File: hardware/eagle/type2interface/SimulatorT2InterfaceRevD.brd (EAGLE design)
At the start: 80 x 80 mm, 25 parts, among them IC1 7805T, IC2 MAX233, IC3 ATMEGA328P_PDIP

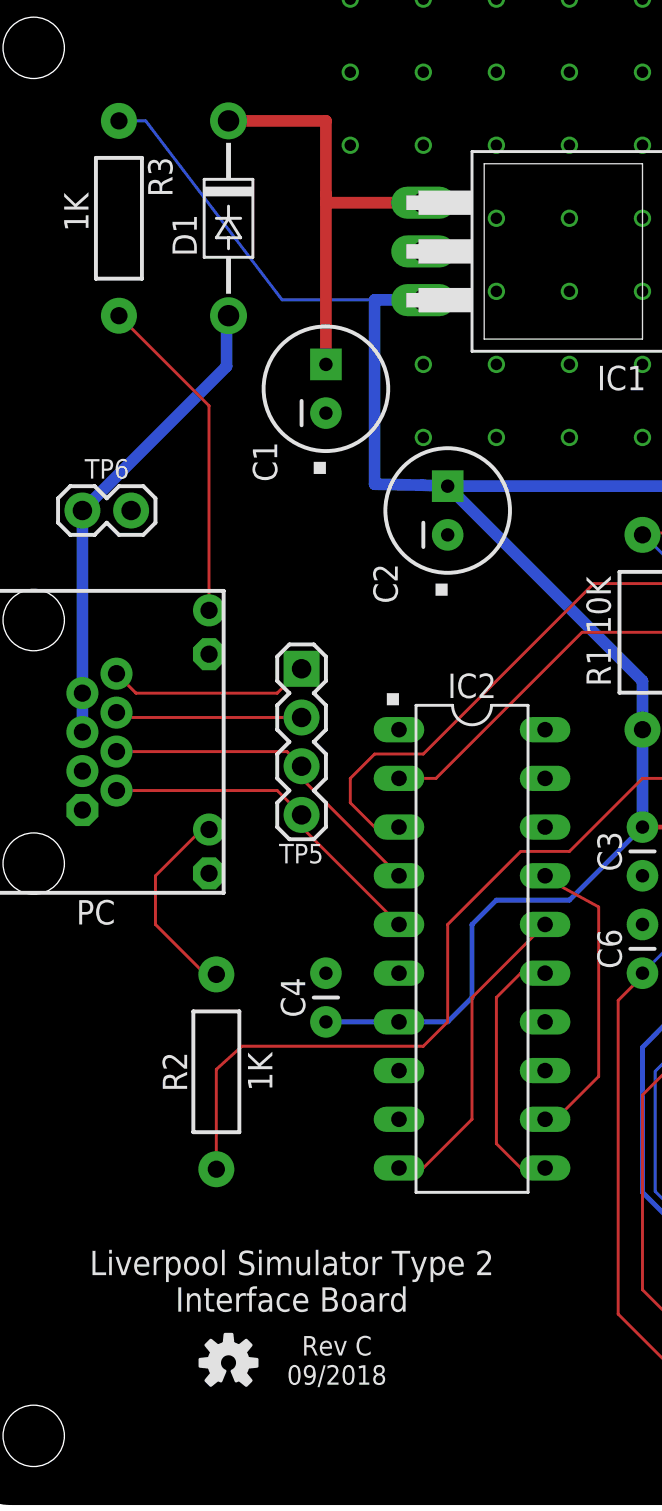
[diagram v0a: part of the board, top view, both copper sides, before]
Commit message: Interface Board Rev D
Fixes a clearance problem with the alternative voltage regulator, and
adds a second serial connection for future use. Enable layer 51 tDocu in
Eagle to see alternate regulator outline. Closes #1
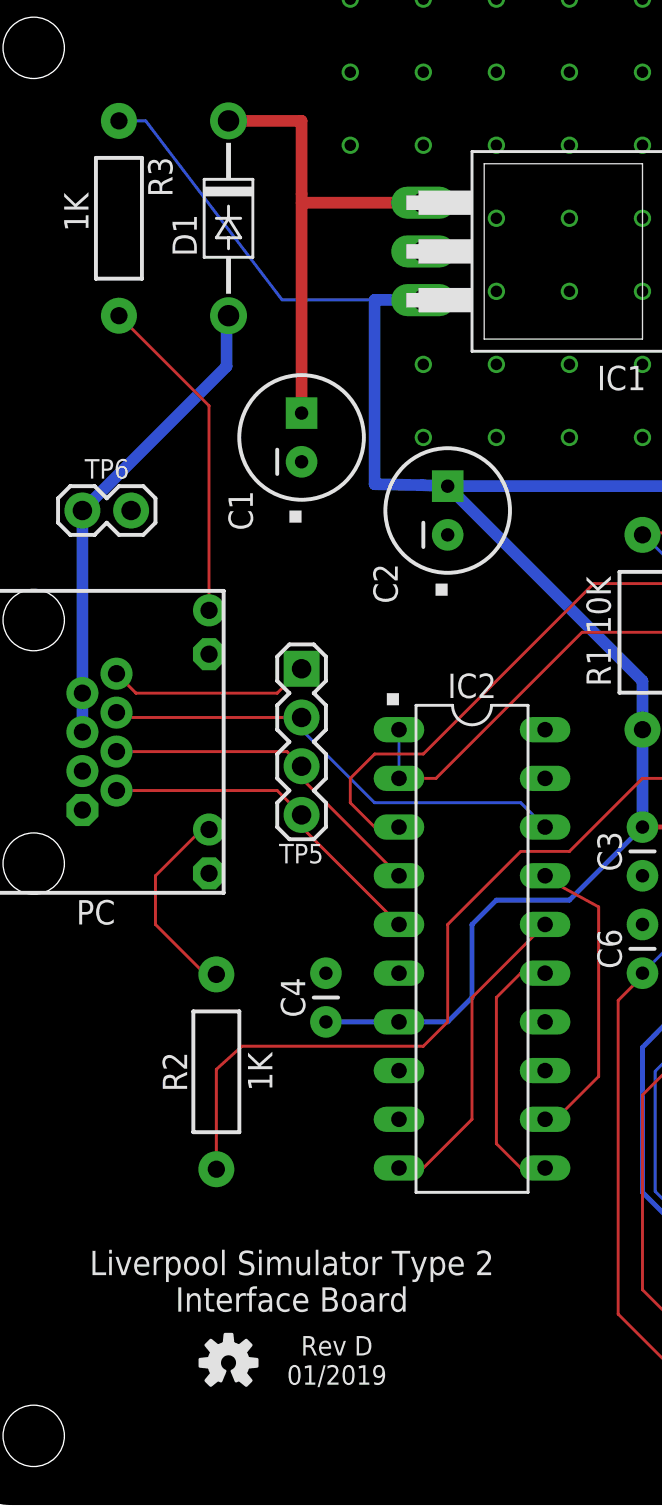
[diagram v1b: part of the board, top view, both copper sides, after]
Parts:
- IC1: device linear:TO220H -> AIC_Custom:TO220H+TSR
- moved C1 2.84 mm to (17.8, 55.9)
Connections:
- removed net P6: PC.6, TP5.2
- new net TX2: IC2.18, PC.6, TP5.2
- net TXD: now also IC2.1
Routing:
- net TX2: track 0.00 -> 24.8 mm
- net P6: track 9.76 -> 0.00 mm
- net VIN2: track 23.3 -> 25.9 mm
- net TXD: track 19.7 -> 22.2 mm
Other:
- board text added: "Rev D 01/2019"
- board text removed: "Rev C 09/2018"
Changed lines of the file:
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@@
 <layer number="49" name="Reference" color="7" fill="1" visible="no" active="yes"/>
 <layer number="50" name="dxf" color="7" fill="1" visible="no" active="no"/>
-<layer number="51" name="tDocu" color="6" fill="1" visible="no" active="yes"/>
+<layer number="51" name="tDocu" color="6" fill="1" visible="yes" active="yes"/>
 <layer number="52" name="bDocu" color="7" fill="1" visible="no" active="yes"/>
 <layer number="53" name="tGND_GNDA" color="7" fill="9" visible="no" active="no"/>
@@
 <text x="17.272" y="10.287" size="1.27" layer="21" font="vector" align="bottom-center">Liverpool Simulator Type 2
 Interface Board</text>
-<text x="19.6215" y="6.477" size="1.016" layer="21" font="vector" align="bottom-center">Rev C
-09/2018</text>
+<text x="19.6215" y="6.477" size="1.016" layer="21" font="vector" align="bottom-center">Rev D
+01/2019</text>
 <rectangle x1="22.225" y1="41.91" x2="22.86" y2="42.545" layer="21"/>
 <rectangle x1="38.735" y1="5.715" x2="39.37" y2="6.35" layer="21"/>
@@
 <dimension x1="80.01" y1="78.74" x2="81.28" y2="78.74" x3="80.645" y3="83.82" textsize="1.27" layer="47"/>
 <rectangle x1="24.765" y1="47.625" x2="25.4" y2="48.26" layer="21" rot="R90"/>
-<rectangle x1="18.415" y1="53.975" x2="19.05" y2="54.61" layer="21" rot="R90"/>
+<rectangle x1="17.145" y1="51.435" x2="17.78" y2="52.07" layer="21" rot="R90"/>
 <dimension x1="-1.27" y1="78.74" x2="0" y2="78.74" x3="-0.635" y3="83.82" textsize="1.27" layer="47"/>
 <hole x="3.81" y="76.2" drill="3.2"/>
@@
 <attribute name="VALUE" x="33.909" y="47.117" size="1.27" layer="21" font="vector" rot="R90" align="bottom-center"/>
 </element>
-<element name="C1" library="SparkFun-Passives" package="CPOL-RADIAL-100UF-25V" value="100uF" x="19.05" y="58.42" smashed="yes" rot="R90">
-<attribute name="VALUE" x="23.9395" y="58.42" size="1.27" layer="27" font="vector" rot="R90" align="bottom-center"/>
-<attribute name="NAME" x="16.51" y="54.61" size="1.27" layer="25" font="vector" rot="R90" align="bottom-center"/>
+<element name="C1" library="SparkFun-Passives" package="CPOL-RADIAL-100UF-25V" value="100uF" x="17.78" y="55.88" smashed="yes" rot="R90">
+<attribute name="VALUE" x="22.6695" y="57.15" size="1.27" layer="27" font="vector" rot="R90" align="bottom-center"/>
+<attribute name="NAME" x="15.24" y="52.07" size="1.27" layer="25" font="vector" rot="R90" align="bottom-center"/>
 </element>
 <element name="C2" library="SparkFun-Passives" package="CPOL-RADIAL-100UF-25V" value="100uF" x="25.4" y="52.07" smashed="yes" rot="R90">
-<attribute name="VALUE" x="30.226" y="52.07" size="1.27" layer="27" font="vector" rot="R90" align="bottom-center"/>
+<attribute name="VALUE" x="30.226" y="53.34" size="1.27" layer="27" font="vector" rot="R90" align="bottom-center"/>
 <attribute name="NAME" x="22.7965" y="48.26" size="1.27" layer="25" font="vector" rot="R90" align="bottom-center"/>
 </element>
@@
 <attribute name="VALUE" x="37.465" y="29.21" size="0.762" layer="27" font="vector" rot="R90" align="bottom-center"/>
 </element>
-<element name="IC1" library="linear" package="TO220H" value="7805T" x="34.29" y="65.5828" smashed="yes" rot="R270">
+<element name="IC1" library="AIC_Custom" package="TO220H+TSR" value="7805T" x="34.29" y="65.5828" smashed="yes" rot="R270">
 <attribute name="NAME" x="34.4678" y="59.6138" size="1.27" layer="25" font="vector" rot="R180" align="bottom-center"/>
 <attribute name="VALUE" x="43.18" y="65.5828" size="1.27" layer="27" font="vector" rot="R270" align="bottom-center"/>
@@
 <wire x1="32.4104" y1="45.72" x2="24.7904" y2="38.1" width="0.1524" layer="1"/>
 <wire x1="39.37" y1="45.72" x2="32.4104" y2="45.72" width="0.1524" layer="1"/>
+<contactref element="IC2" pad="1"/>
+<wire x1="22.86" y1="40.64" x2="22.86" y2="38.1" width="0.1524" layer="16"/>
 </signal>
 <signal name="N$9">
@@
 <contactref element="D1" pad="C"/>
 <wire x1="14.0208" y1="72.39" x2="13.97" y2="72.39" width="0.1524" layer="1"/>
-<wire x1="14.0208" y1="72.39" x2="19.05" y2="72.39" width="0.6096" layer="1"/>
-<wire x1="19.05" y1="72.39" x2="19.05" y2="68.58" width="0.6096" layer="1"/>
-<wire x1="19.05" y1="68.58" x2="19.05" y2="59.69" width="0.6096" layer="1"/>
-<wire x1="24.13" y1="68.1228" x2="19.05" y2="68.1228" width="0.6096" layer="1"/>
-<wire x1="19.05" y1="68.1228" x2="19.05" y2="68.58" width="0.4064" layer="1"/>
+<wire x1="14.0208" y1="72.39" x2="17.78" y2="72.39" width="0.6096" layer="1"/>
+<wire x1="17.78" y1="72.39" x2="17.78" y2="68.58" width="0.6096" layer="1"/>
+<wire x1="17.78" y1="68.58" x2="17.78" y2="57.15" width="0.6096" layer="1"/>
+<wire x1="24.13" y1="68.1228" x2="17.78" y2="68.1228" width="0.6096" layer="1"/>
+<wire x1="17.78" y1="68.1228" x2="17.78" y2="68.58" width="0.4064" layer="1"/>
 </signal>
 <signal name="N$17">
@@
 <wire x1="59.182" y1="12.827" x2="71.882" y2="12.827" width="0.1524" layer="1"/>
 </signal>
-<signal name="P6">
-<contactref element="TP5" pad="2"/>
-<contactref element="PC" pad="6"/>
-<wire x1="8.128" y1="41.529" x2="8.382" y2="41.275" width="0.1524" layer="1"/>
-<wire x1="8.382" y1="41.275" x2="17.78" y2="41.275" width="0.1524" layer="1"/>
-</signal>
 <signal name="P8">
 <contactref element="TP5" pad="1"/>
@@
 <wire x1="55.245" y1="36.83" x2="58.42" y2="40.005" width="0.1524" layer="1"/>
 </signal>
+<signal name="TX2">
+<contactref element="IC2" pad="18"/>
+<contactref element="PC" pad="6"/>
+<contactref element="TP5" pad="2"/>
+<wire x1="8.382" y1="41.275" x2="17.78" y2="41.275" width="0.1524" layer="1"/>
+<wire x1="30.48" y1="35.56" x2="29.21" y2="36.83" width="0.1524" layer="16"/>
+<wire x1="29.21" y1="36.83" x2="21.59" y2="36.83" width="0.1524" layer="16"/>
+<wire x1="21.59" y1="36.83" x2="17.78" y2="40.64" width="0.1524" layer="16"/>
+<wire x1="17.78" y1="40.64" x2="17.78" y2="41.275" width="0.1524" layer="16"/>
+<wire x1="8.382" y1="41.275" x2="8.128" y2="41.529" width="0" layer="19" extent="1-1"/>
+</signal>
 </signals>
+<errors>
+</errors>
 </board>
 </drawing>
